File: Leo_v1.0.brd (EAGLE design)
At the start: 68.6 x 53.3 mm, 56 parts, among them CN1 POWER_JACK, CN2 47346-0001, CN3 DIGITAL10, CN4 DIGITAL8, CN5 ICSP, CN6 POWER8, CN7 ANALOG6, IC1 AMS1117-5.0, IC2 AMS1117-3.3, IC3 MCP6002T-I/SN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

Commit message: Use LM358D OpAmp instead.
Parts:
- IC3: value MCP6002T-I/SN -> LM358D
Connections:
- removed net N$1: IC3.5, IC3.7
- net GND: now also IC3.5
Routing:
- net N$1: track 5.81 -> 0.00 mm, vias 2 -> 0
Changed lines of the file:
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@@
 <drawing>
 <settings>
-<setting alwaysvectorfont="yes"/>
+<setting alwaysvectorfont="no"/>
 <setting verticaltext="up"/>
 </settings>
@@
 <attribute name="VALUE" x="11.176" y="37.592" size="0.6096" layer="27" font="vector"/>
 </element>
-<element name="IC3" library="linear" library_urn="urn:adsk.eagle:library:262" package="SO08" package3d_urn="urn:adsk.eagle:package:16404/2" value="MCP6002T-I/SN" x="9.906" y="26.162" smashed="yes" rot="R90">
+<element name="IC3" library="linear" library_urn="urn:adsk.eagle:library:262" package="SO08" package3d_urn="urn:adsk.eagle:package:16404/2" value="LM358D" x="9.906" y="26.162" smashed="yes" rot="R90">
 <attribute name="NAME" x="8.509" y="27.559" size="0.6096" layer="27" font="vector"/>
 <attribute name="POPULARITY" value="4" x="9.906" y="26.162" size="1.778" layer="27" rot="R90" display="off"/>
@@
 <via x="54.864" y="5.334" extent="1-16" drill="0.35"/>
 <via x="38.608" y="45.847" extent="1-16" drill="0.35"/>
+<contactref element="IC3" pad="5"/>
 </signal>
 <signal name="VIN" class="3">
@@
 <wire x1="11.303" y1="29.972" x2="10.406" y2="29.972" width="0.3048" layer="1"/>
 </signal>
-<signal name="N$1">
-<contactref element="IC3" pad="5"/>
-<contactref element="IC3" pad="7"/>
-<wire x1="7.306" y1="25.527" x2="8.9408" y2="25.527" width="0.3048" layer="1"/>
-<via x="8.9408" y="25.527" extent="1-16" drill="0.35"/>
-<via x="8.938" y="28.067" extent="1-16" drill="0.35"/>
-<wire x1="8.938" y1="28.067" x2="8.938" y2="25.5298" width="0.3048" layer="16"/>
-<wire x1="8.9408" y1="25.527" x2="8.938" y2="25.5298" width="0.3048" layer="16"/>
-<wire x1="8.938" y1="28.067" x2="7.306" y2="28.067" width="0.3048" layer="1"/>
-</signal>
 <signal name="MCU_OSC_IN">

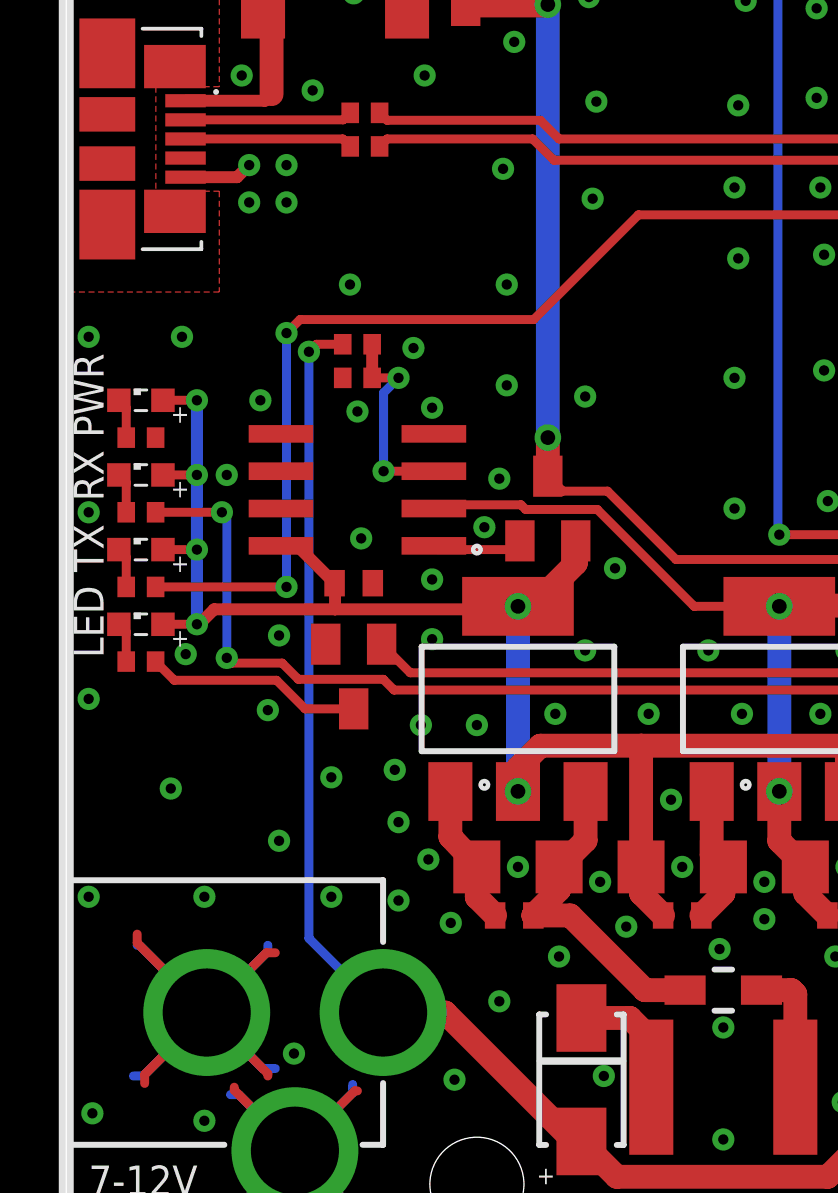
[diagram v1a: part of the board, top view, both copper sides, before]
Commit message: Properly disabled second channel of op amp.
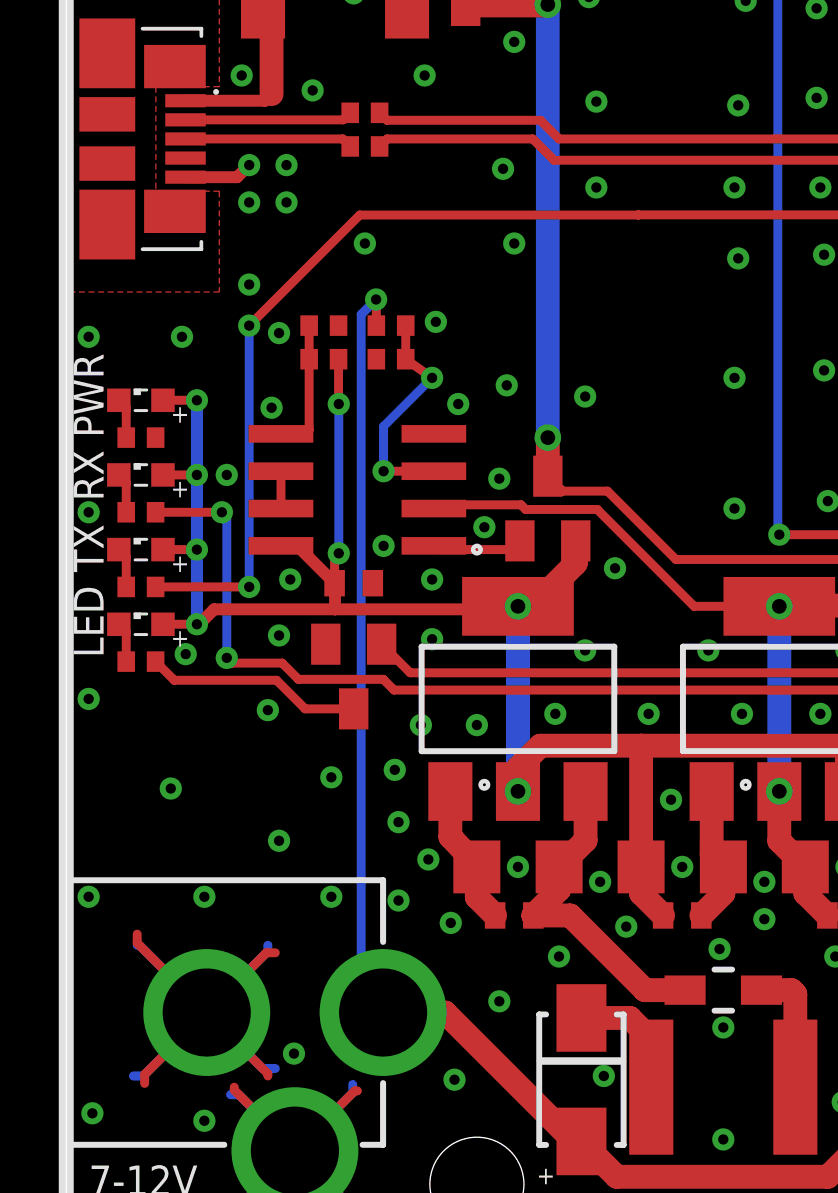
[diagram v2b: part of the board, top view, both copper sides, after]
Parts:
- added R11, R13: 100K, rcl:R0402
- moved R4 1.31 mm to (11.0, 31.8)
- moved R5 1.31 mm to (11.0, 30.6)
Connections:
- new net N$1: IC3.5, R11.1, R13.2
- new net N$6: IC3.6, IC3.7
- net 5V: now also R11.2
- net GND: now also R13.1; no longer IC3.5, IC3.6
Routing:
- net 5V: track 195.7 -> 203.4 mm, vias 14 -> 16
- net N$1: track 0.00 -> 4.56 mm
- net N$6: track 0.00 -> 1.27 mm
- net VIN: track 65.2 -> 66.1 mm
- net N$12: track 7.14 -> 7.81 mm
- net GND: vias 224 -> 226

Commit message: Created new routing.
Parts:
- moved Q2 9.68 mm to (60.1, 41.1), turned to 315 degrees
- moved C13 8.40 mm to (57.5, 40.6), turned to 315 degrees
- moved C17 8.11 mm to (61.9, 36.5), turned to 135 degrees
- moved C12 7.90 mm to (59.5, 38.7), turned to 135 degrees
- moved C16 7.26 mm to (42.6, 28.8), turned to 225 degrees
- moved R6 6.95 mm to (57.9, 38.3), turned to 315 degrees
- moved R3 6.95 mm to (43.7, 33.0), turned to 135 degrees
- moved C15 6.72 mm to (59.9, 36.2), turned to 135 degrees
- moved R12 6.02 mm to (59.9, 34.5), turned to 315 degrees
- moved C14 5.77 mm to (55.5, 23.5), turned to 315 degrees
- moved C9 5.59 mm to (49.3, 24.1), turned to 135 degrees
- moved C19 5.45 mm to (48.2, 23.0), turned to 315 degrees
- moved C7 5.41 mm to (58.3, 25.5), turned to 315 degrees
- moved L3 4.74 mm to (53.0, 21.8), turned to 45 degrees
- moved U1 1.53 mm to (51.7, 32.1), turned to 135 degrees
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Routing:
- net D11_MOSI: track 82.5 -> 42.2 mm, vias 3 -> 2
- net 5V: track 203.4 -> 181.6 mm, vias 16 -> 12
- net AREF: track 63.2 -> 42.7 mm, vias 1 -> 2
- net TX_LED: track 58.3 -> 76.1 mm, vias 2 -> 4
- net AVCC: track 28.8 -> 45.5 mm
- net D1_TX: track 32.1 -> 18.3 mm, vias 2 -> 0
- net D6_PWM: track 31.6 -> 18.2 mm, vias 2 -> 0
- net D0_RX: track 32.9 -> 19.5 mm, vias 2 -> 0
- net D5_PWM: track 36.0 -> 22.7 mm
- net D4: track 31.3 -> 18.0 mm, vias 2 -> 0
- net D3_SCL: track 55.3 -> 67.8 mm, vias 2 -> 3
- net RESET: track 138.1 -> 125.9 mm, vias 4 -> 2
- net A0: track 26.1 -> 38.0 mm, vias 1 -> 0
- net D7: track 36.9 -> 48.7 mm, vias 1 -> 2
- net A1: track 26.7 -> 37.4 mm, vias 1 -> 0
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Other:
- board text added: "LEO/32U4 v1.0 (c) Andriy Golovnya Designed in Germany http://redscorp.net"
- board text removed: "Leo v1.0 (c) Andriy Golovnya Designed in Germany http://redscorp.net"

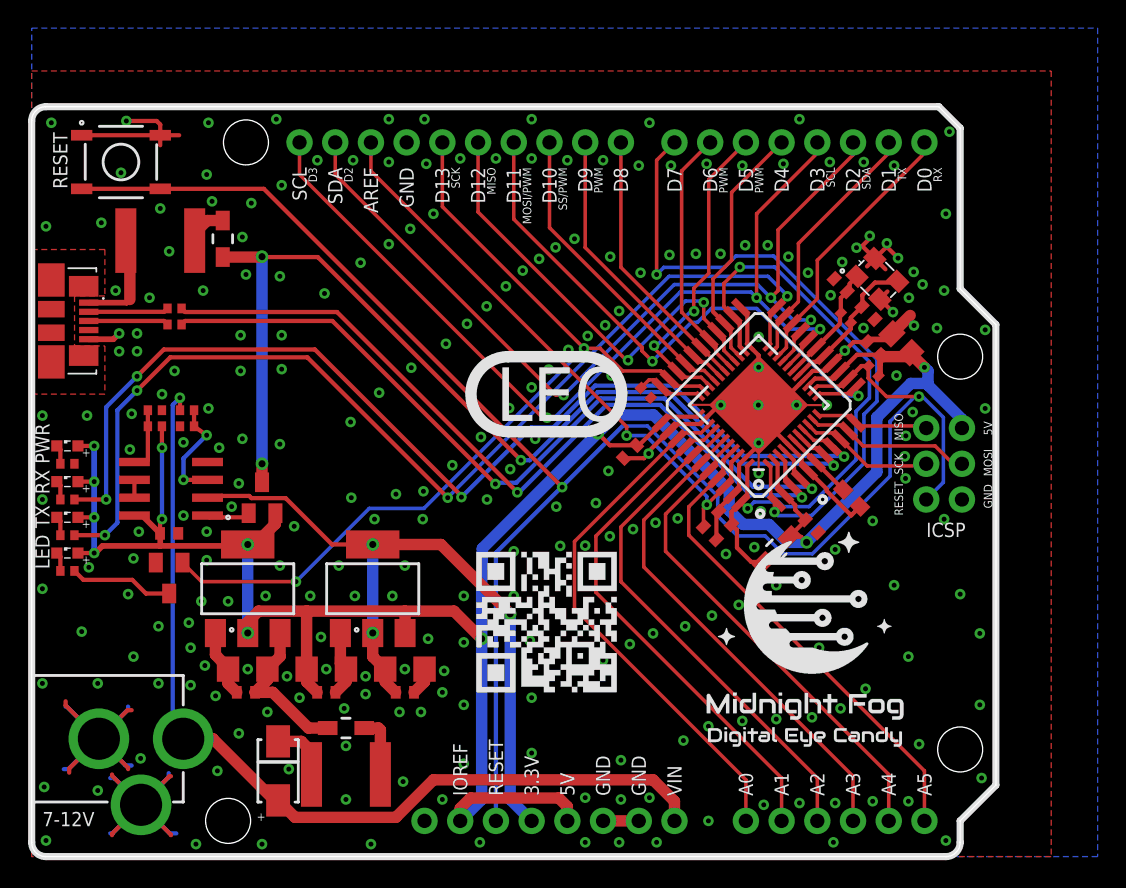
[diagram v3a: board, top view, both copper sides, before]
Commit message: Moved some traces around
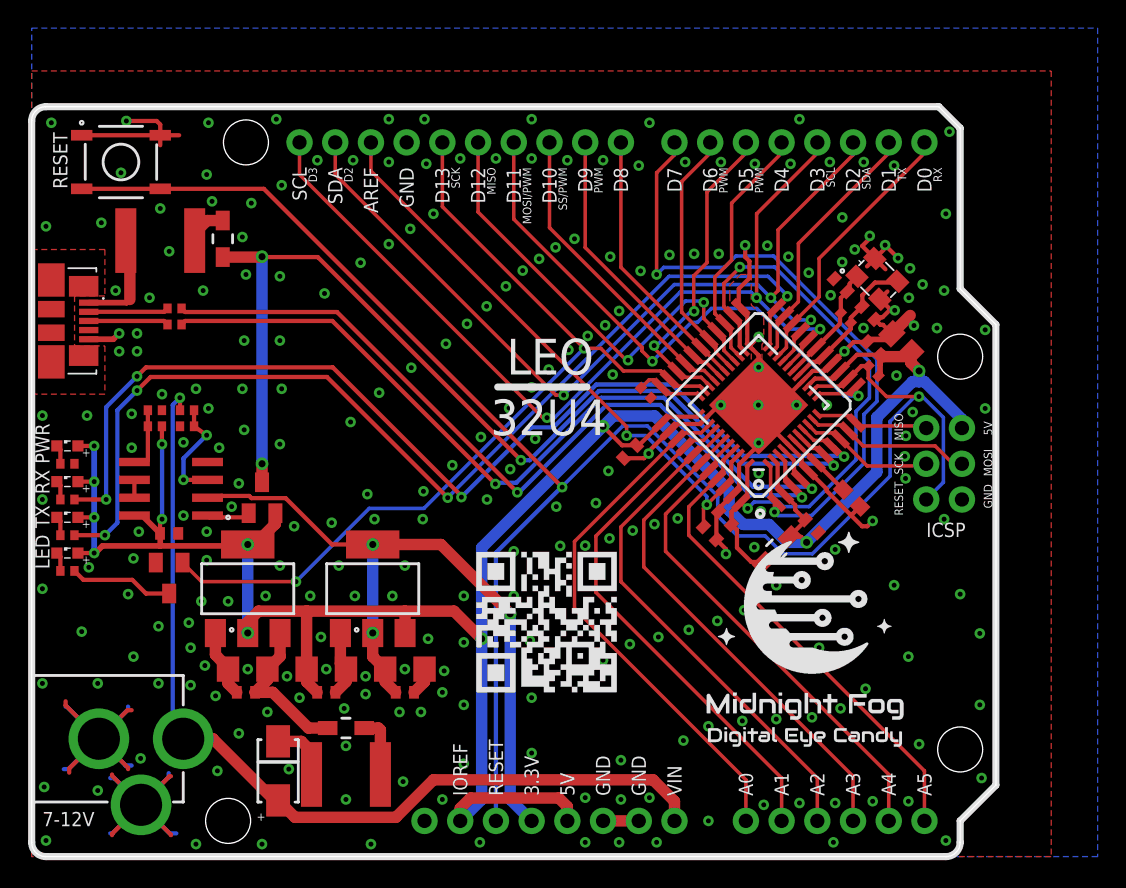
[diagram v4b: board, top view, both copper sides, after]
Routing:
- net GND: track 134.8 -> 141.1 mm, vias 259 -> 260
- net TX_LED: track 76.1 -> 74.9 mm
- net RX_LED: track 76.6 -> 75.6 mm
- net 5V: track 181.6 -> 180.8 mm
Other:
- board text added: "32U4"

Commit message: Moved some traces around
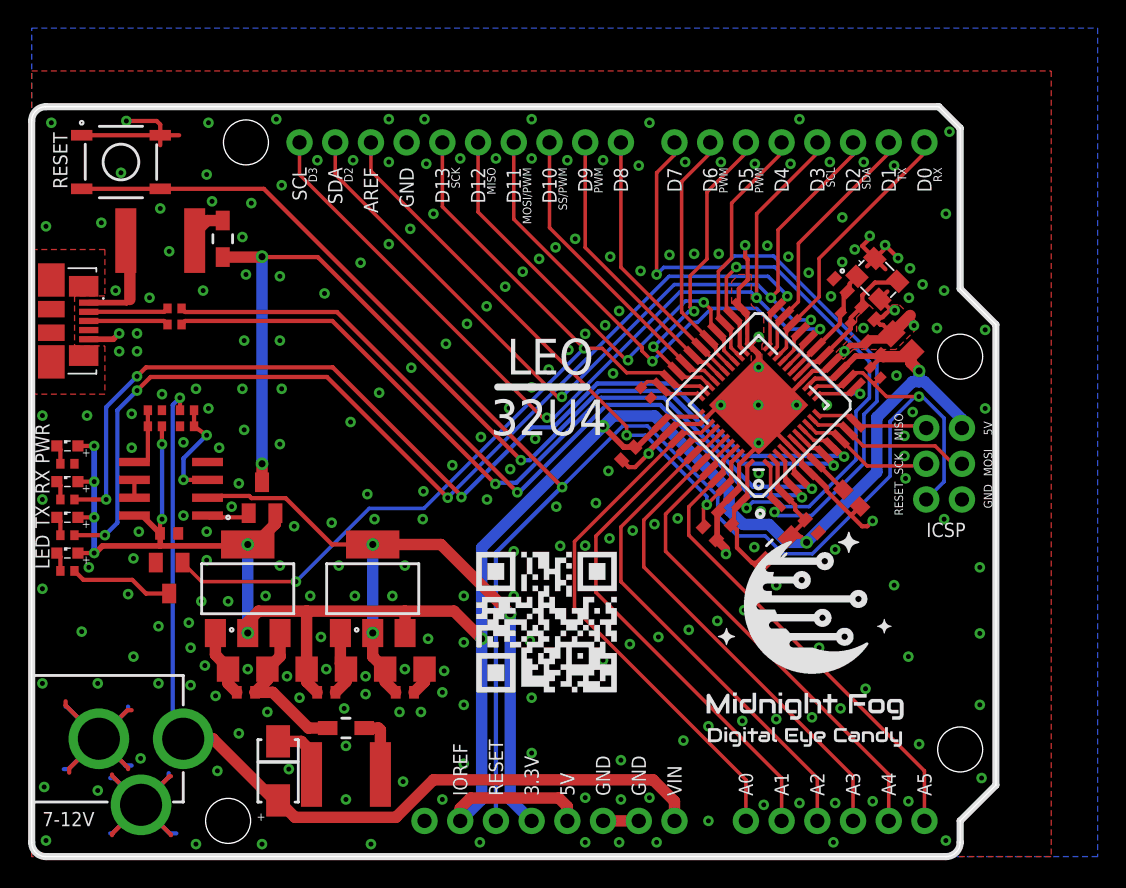
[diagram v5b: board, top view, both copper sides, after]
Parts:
- moved C16 0.18 mm to (42.4, 28.7)
- moved R12 0.17 mm to (60.0, 34.4), turned to 135 degrees
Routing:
- net GND: track 141.1 -> 141.7 mm

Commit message: Renamed U1 into U3 for naming consistency
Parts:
- renumbered U1 to U3

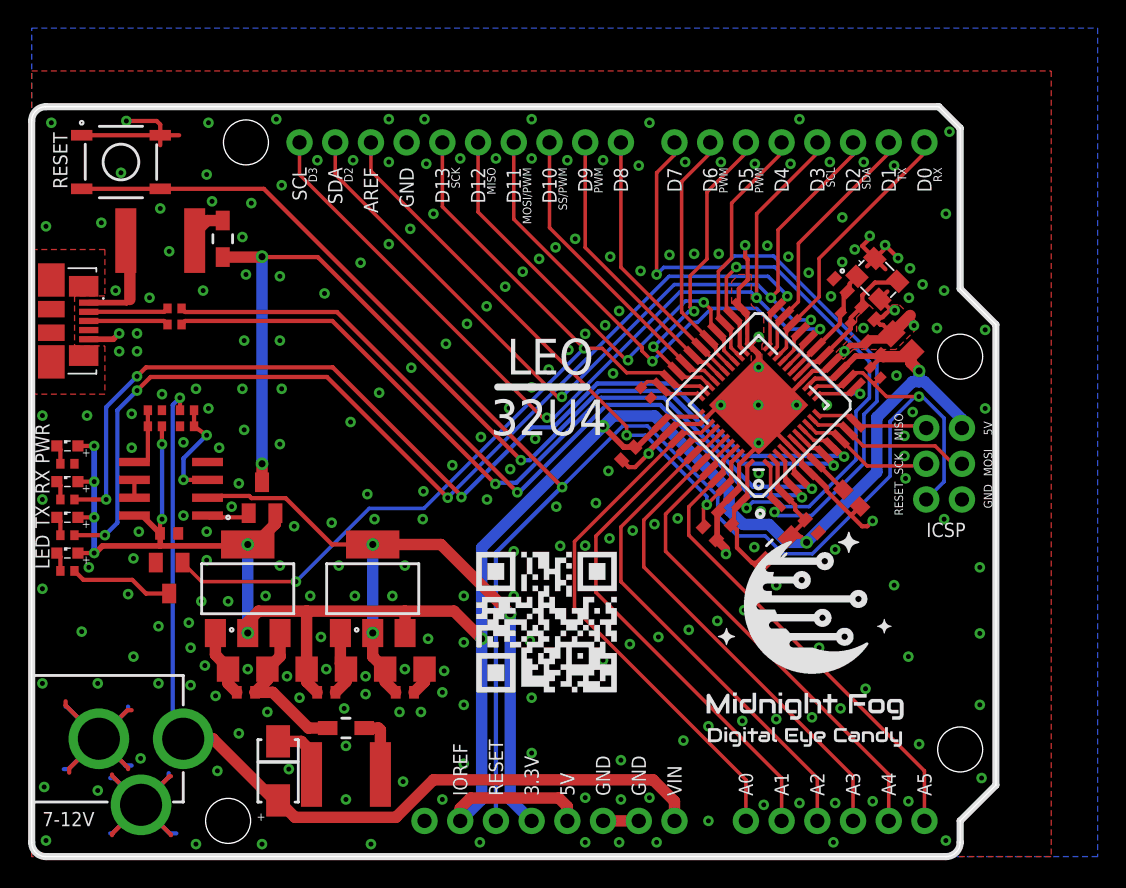
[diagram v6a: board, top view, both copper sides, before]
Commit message: Added tooling holes for JLCPCB. Generated PNG preview. Generated PDF schematics.
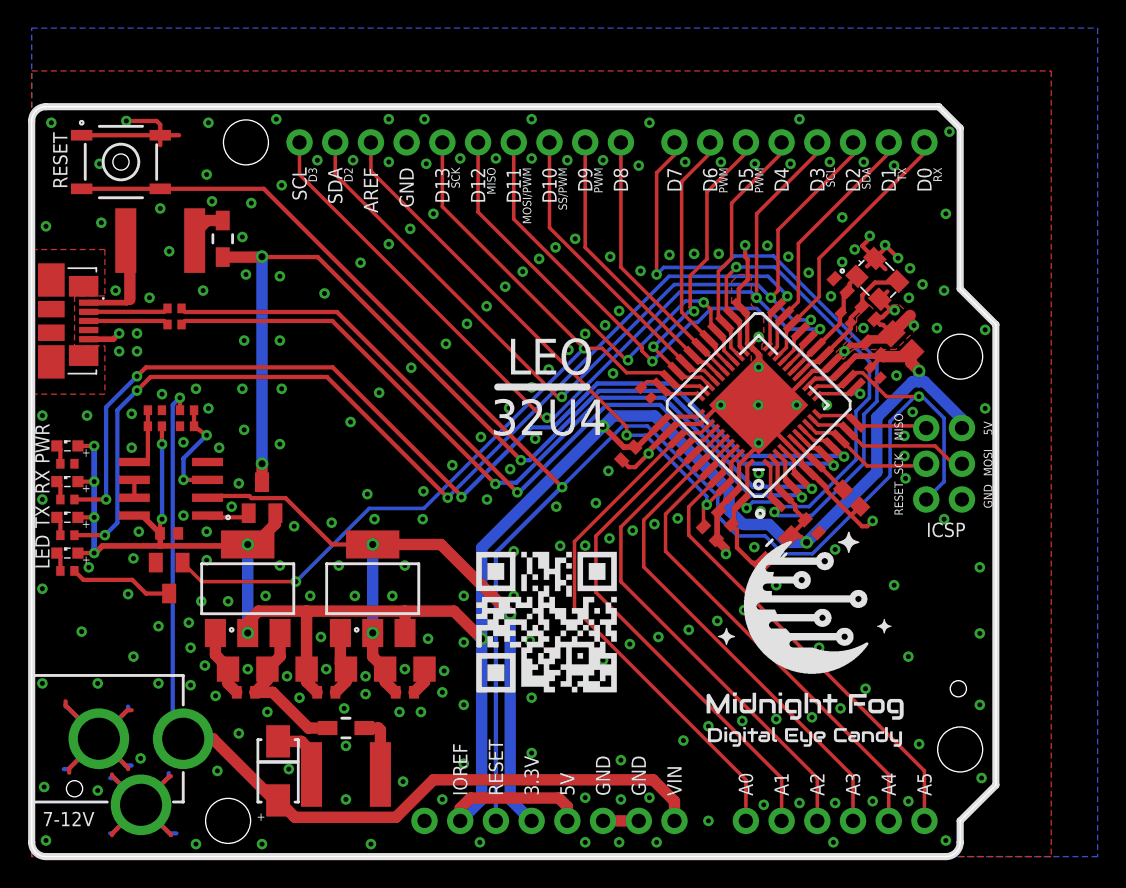
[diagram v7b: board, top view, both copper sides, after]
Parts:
- added HOLE1, HOLE2, HOLE3: TOOLINGHOLE, _my_fiducia:TOOLING-HOLE
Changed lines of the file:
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@@
 <drawing>
 <settings>
-<setting alwaysvectorfont="yes"/>
+<setting alwaysvectorfont="no"/>
 <setting verticaltext="up"/>
 </settings>
@@
 <attribute name="VALUE" x="5.842" y="31.369" size="0.6096" layer="27" font="vector"/>
 </element>
+<element name="HOLE1" library="_my_fiducia" package="TOOLING-HOLE" value="TOOLINGHOLE" x="6.35" y="49.403" smashed="yes"/>
+<element name="HOLE2" library="_my_fiducia" package="TOOLING-HOLE" value="TOOLINGHOLE" x="3.048" y="4.826" smashed="yes"/>
+<element name="HOLE3" library="_my_fiducia" package="TOOLING-HOLE" value="TOOLINGHOLE" x="65.913" y="11.938" smashed="yes"/>
 </elements>
 <signals>
@@
 <via x="6.223" y="35.941" extent="1-16" drill="0.35"/>
 <via x="12.446" y="48.514" extent="1-16" drill="0.35"/>
-<via x="6.35" y="48.641" extent="1-16" drill="0.35"/>
+<via x="4.826" y="49.276" extent="1-16" drill="0.35"/>
 <via x="1.397" y="52.197" extent="1-16" drill="0.35"/>
 <via x="22.352" y="4.064" extent="1-16" drill="0.35"/>
